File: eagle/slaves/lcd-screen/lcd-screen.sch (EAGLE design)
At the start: 25 parts, among them CON1 SPI, IC1 MCP1703CB, J1 RJ12RIGHTANGLE-I2C, J2 RJ12RIGHTANGLE-I2C, J3 RJ12RIGHTANGLE-I2C, U1 ATMEGA328P_TQFP

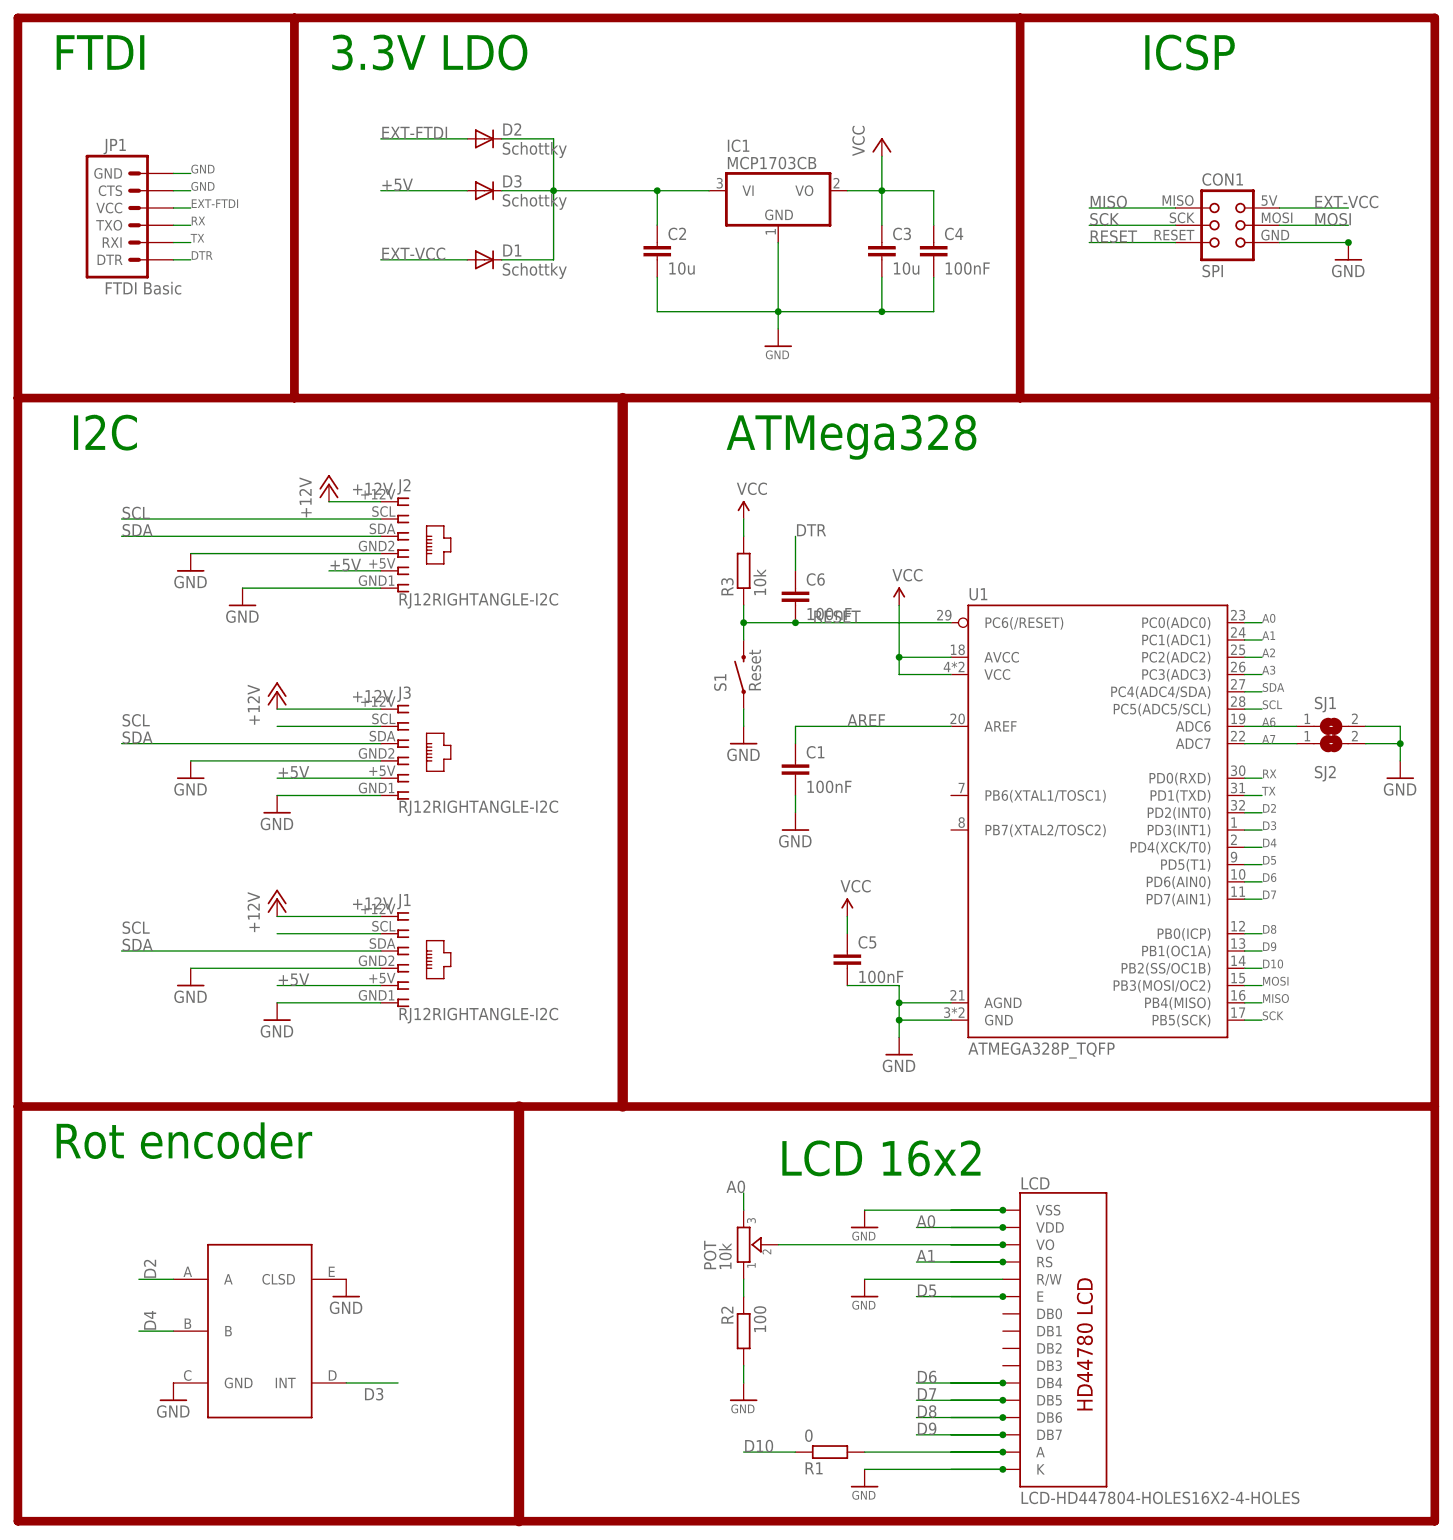
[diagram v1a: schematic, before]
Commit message: add crystal to bard
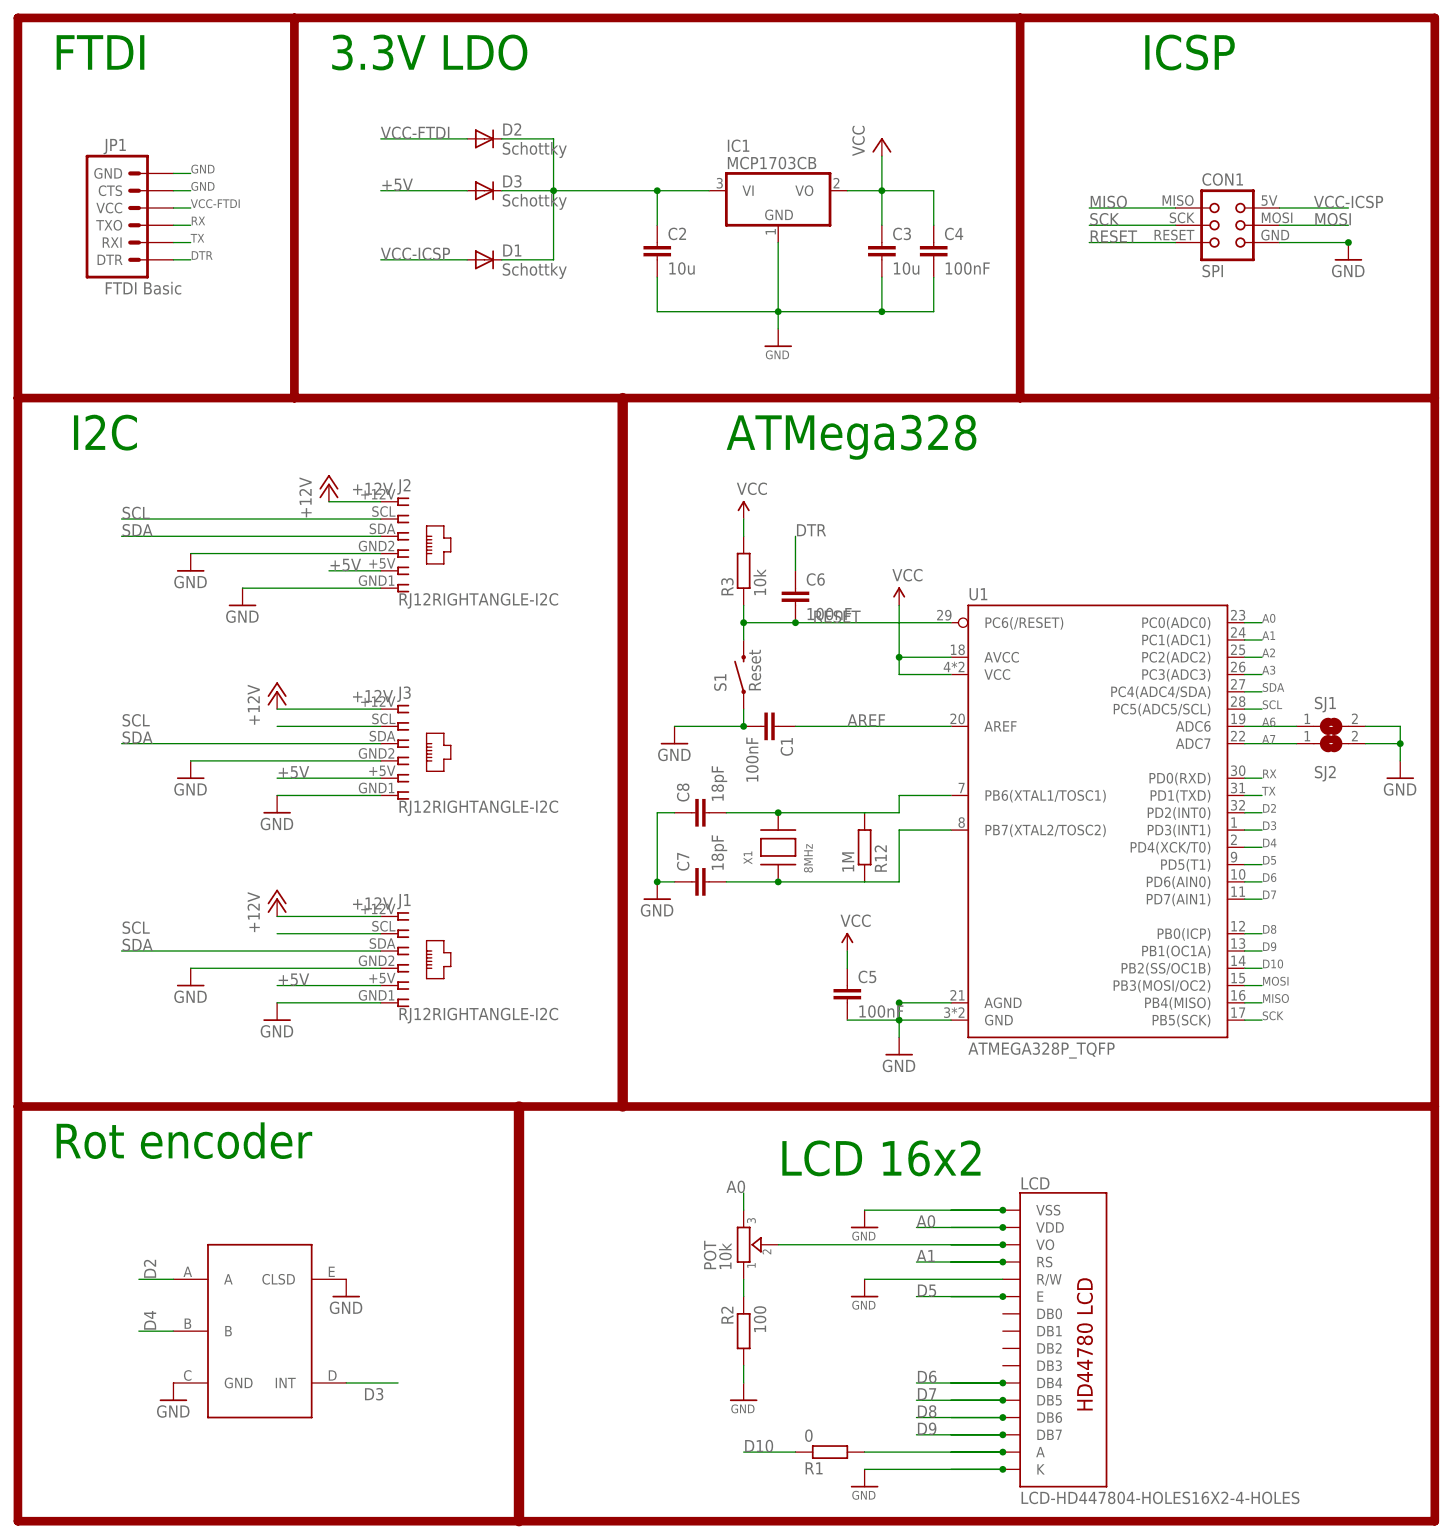
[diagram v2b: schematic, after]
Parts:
- added C7, C8: 18pF, rcl:C-EUC0805K
- added R12: 1M, rcl:R-EU_R0805
- added X1: 8MHz, lpatiny:XTALNX6035
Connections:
- net EXT-FTDI renamed VCC-FTDI
- net EXT-VCC renamed VCC-ICSP
- new net N$42: C8.2, R12.2, U1.PB6(XTAL1/TOSC1), X1.P$2
- new net XTAL1: C7.2, R12.1, U1.PB7(XTAL2/TOSC2), X1.P$1
- net GND: now also C7.1, C8.1
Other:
- moved on the sheet: C1, C5
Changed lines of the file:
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@@
 </part>
 <part name="GND3" library="SparkFun" deviceset="GND" device=""/>
-<part name="GND7" library="SparkFun" deviceset="GND" device=""/>
 <part name="P+11" library="SparkFun" deviceset="3.3V" device="" value="VCC"/>
 <part name="P+2" library="SparkFun" deviceset="3.3V" device="" value="VCC"/>
@@
 <part name="SJ2" library="jumper" library_urn="urn:adsk.eagle:library:252" deviceset="SJ" device="" package3d_urn="urn:adsk.eagle:package:15471/1"/>
 <part name="GND13" library="SparkFun" deviceset="GND" device=""/>
+<part name="C7" library="rcl" library_urn="urn:adsk.eagle:library:334" deviceset="C-EU" device="C0805K" package3d_urn="urn:adsk.eagle:package:23681/2" value="18pF">
+<attribute name="ELECROW" value="C1797"/>
+<attribute name="LCSC" value="C1797"/>
+<attribute name="MPN" value="77-VJ1206A180JXXPBC"/>
+</part>
+<part name="C8" library="rcl" library_urn="urn:adsk.eagle:library:334" deviceset="C-EU" device="C0805K" package3d_urn="urn:adsk.eagle:package:23681/2" value="18pF">
+<attribute name="ELECROW" value="C1797"/>
+<attribute name="LCSC" value="C1797"/>
+<attribute name="MPN" value="77-VJ1206A180JXXPBC"/>
+</part>
+<part name="X1" library="lpatiny" deviceset="XTAL" device="NX6035" value="8MHz">
+<attribute name="LCSC" value="C122522"/>
+<attribute name="MPN" value="729-F60800010"/>
+</part>
+<part name="GND39" library="supply1" deviceset="GND" device=""/>
+<part name="R12" library="rcl" deviceset="R-EU_" device="R0805" value="1M">
+<attribute name="ELECROW" value="C17514"/>
+<attribute name="LCSC" value="C17514"/>
+</part>
 </parts>
 <sheets>
@@
 <attribute name="LCSC" x="111.76" y="195.58" size="1.778" layer="96" display="off"/>
 </instance>
-<instance part="GND3" gate="1" x="106.68" y="114.3"/>
-<instance part="GND7" gate="1" x="114.3" y="101.6"/>
+<instance part="GND3" gate="1" x="96.52" y="114.3"/>
 <instance part="P+11" gate="G$1" x="106.68" y="147.32"/>
 <instance part="P+2" gate="G$1" x="129.54" y="134.62"/>
@@
 <attribute name="ELECROW" x="114.3" y="137.16" size="1.778" layer="96" display="off"/>
 </instance>
-<instance part="C1" gate="G$1" x="114.3" y="111.76">
-<attribute name="MPN" x="114.3" y="111.76" size="1.778" layer="96" display="off"/>
-<attribute name="LCSC" x="114.3" y="111.76" size="1.778" layer="96" display="off"/>
-<attribute name="ELECROW" x="114.3" y="111.76" size="1.778" layer="96" display="off"/>
-</instance>
-<instance part="C5" gate="G$1" x="121.92" y="83.82">
-<attribute name="MPN" x="121.92" y="83.82" size="1.778" layer="96" display="off"/>
-<attribute name="LCSC" x="121.92" y="83.82" size="1.778" layer="96" display="off"/>
-<attribute name="ELECROW" x="121.92" y="83.82" size="1.778" layer="96" display="off"/>
-</instance>
-<instance part="P+3" gate="G$1" x="121.92" y="88.9"/>
+<instance part="C1" gate="G$1" x="111.76" y="116.84" rot="R270">
+<attribute name="MPN" x="111.76" y="116.84" size="1.778" layer="96" rot="R270" display="off"/>
+<attribute name="LCSC" x="111.76" y="116.84" size="1.778" layer="96" rot="R270" display="off"/>
+<attribute name="ELECROW" x="111.76" y="116.84" size="1.778" layer="96" rot="R270" display="off"/>
+</instance>
+<instance part="C5" gate="G$1" x="121.92" y="78.74">
+<attribute name="MPN" x="121.92" y="78.74" size="1.778" layer="96" display="off"/>
+<attribute name="LCSC" x="121.92" y="78.74" size="1.778" layer="96" display="off"/>
+<attribute name="ELECROW" x="121.92" y="78.74" size="1.778" layer="96" display="off"/>
+</instance>
+<instance part="P+3" gate="G$1" x="121.92" y="83.82"/>
 <instance part="R3" gate="G$1" x="106.68" y="139.7" rot="R90">
 <attribute name="LCSC" x="106.68" y="139.7" size="1.778" layer="96" rot="R90" display="off"/>
@@
 </instance>
 <instance part="GND13" gate="1" x="203.2" y="109.22"/>
+<instance part="C7" gate="G$1" x="99.06" y="93.98" rot="R90">
+<attribute name="MPN" x="99.06" y="93.98" size="1.778" layer="96" rot="R90" display="off"/>
+<attribute name="LCSC" x="99.06" y="93.98" size="1.778" layer="96" rot="R90" display="off"/>
+<attribute name="ELECROW" x="99.06" y="93.98" size="1.778" layer="96" rot="R90" display="off"/>
+</instance>
+<instance part="C8" gate="G$1" x="99.06" y="104.14" rot="R90">
+<attribute name="MPN" x="99.06" y="104.14" size="1.778" layer="96" rot="R90" display="off"/>
+<attribute name="LCSC" x="99.06" y="104.14" size="1.778" layer="96" rot="R90" display="off"/>
+<attribute name="ELECROW" x="99.06" y="104.14" size="1.778" layer="96" rot="R90" display="off"/>
+</instance>
+<instance part="X1" gate="G$1" x="111.76" y="99.06" rot="R90">
+<attribute name="MPN" x="111.76" y="99.06" size="1.778" layer="96" rot="R90" display="off"/>
+<attribute name="LCSC" x="111.76" y="99.06" size="1.778" layer="96" rot="R90" display="off"/>
+</instance>
+<instance part="GND39" gate="1" x="93.98" y="91.44"/>
+<instance part="R12" gate="G$1" x="124.46" y="99.06" rot="MR90">
+<attribute name="ELECROW" x="124.46" y="99.06" size="1.778" layer="96" rot="MR90" display="off"/>
+<attribute name="LCSC" x="124.46" y="99.06" size="1.778" layer="96" rot="MR90" display="off"/>
+</instance>
 </instances>
 <busses>
@@
 </segment>
 <segment>
-<wire x1="106.68" y1="119.38" x2="106.68" y2="116.84" width="0.1524" layer="91"/>
 <pinref part="GND3" gate="1" pin="GND"/>
 <pinref part="S1" gate="G$1" pin="1"/>
-</segment>
-<segment>
-<wire x1="114.3" y1="104.14" x2="114.3" y2="106.68" width="0.1524" layer="91"/>
-<pinref part="GND7" gate="1" pin="GND"/>
 <pinref part="C1" gate="G$1" pin="2"/>
-</segment>
-<segment>
-<wire x1="129.54" y1="78.74" x2="129.54" y2="76.2" width="0.1524" layer="91"/>
+<wire x1="96.52" y1="116.84" x2="106.68" y2="116.84" width="0.1524" layer="91"/>
+<wire x1="106.68" y1="116.84" x2="106.68" y2="119.38" width="0.1524" layer="91"/>
+<junction x="106.68" y="116.84"/>
+</segment>
+<segment>
 <pinref part="GND5" gate="1" pin="GND"/>
 <pinref part="C5" gate="G$1" pin="2"/>
 <wire x1="129.54" y1="76.2" x2="129.54" y2="73.66" width="0.1524" layer="91"/>
 <wire x1="129.54" y1="73.66" x2="129.54" y2="71.12" width="0.1524" layer="91"/>
-<wire x1="129.54" y1="78.74" x2="121.92" y2="78.74" width="0.1524" layer="91"/>
+<wire x1="129.54" y1="73.66" x2="121.92" y2="73.66" width="0.1524" layer="91"/>
 <pinref part="U1" gate="U1" pin="GND"/>
 <wire x1="137.16" y1="73.66" x2="129.54" y2="73.66" width="0.1524" layer="91"/>
@@
 <wire x1="198.12" y1="114.3" x2="203.2" y2="114.3" width="0.1524" layer="91"/>
 <junction x="203.2" y="114.3"/>
+</segment>
+<segment>
+<pinref part="C8" gate="G$1" pin="1"/>
+<wire x1="96.52" y1="104.14" x2="93.98" y2="104.14" width="0.1524" layer="91"/>
+<pinref part="C7" gate="G$1" pin="1"/>
+<wire x1="93.98" y1="104.14" x2="93.98" y2="93.98" width="0.1524" layer="91"/>
+<wire x1="93.98" y1="93.98" x2="96.52" y2="93.98" width="0.1524" layer="91"/>
+<pinref part="GND39" gate="1" pin="GND"/>
+<junction x="93.98" y="93.98"/>
 </segment>
 </net>
@@
 <pinref part="C5" gate="G$1" pin="1"/>
 <pinref part="P+3" gate="G$1" pin="3.3V"/>
-<wire x1="121.92" y1="86.36" x2="121.92" y2="88.9" width="0.1524" layer="91"/>
+<wire x1="121.92" y1="81.28" x2="121.92" y2="83.82" width="0.1524" layer="91"/>
 </segment>
 </net>
@@
 <segment>
 <wire x1="137.16" y1="116.84" x2="114.3" y2="116.84" width="0.1524" layer="91"/>
-<wire x1="114.3" y1="116.84" x2="114.3" y2="114.3" width="0.1524" layer="91"/>
 <label x="121.92" y="116.84" size="1.778" layer="95"/>
 <pinref part="C1" gate="G$1" pin="1"/>
@@
 </segment>
 </net>
-<net name="EXT-VCC" class="0">
+<net name="VCC-ICSP" class="0">
 <segment>
 <pinref part="D1" gate="G$1" pin="A"/>
@@
 </segment>
 </net>
-<net name="EXT-FTDI" class="0">
+<net name="VCC-FTDI" class="0">
 <segment>
 <pinref part="D2" gate="G$1" pin="A"/>
@@
 </segment>
 </net>
+<net name="XTAL1" class="0">
+<segment>
+<pinref part="C7" gate="G$1" pin="2"/>
+<wire x1="124.46" y1="93.98" x2="111.76" y2="93.98" width="0.1524" layer="91"/>
+<wire x1="111.76" y1="93.98" x2="104.14" y2="93.98" width="0.1524" layer="91"/>
+<pinref part="X1" gate="G$1" pin="P$1"/>
+<junction x="111.76" y="93.98"/>
+<pinref part="R12" gate="G$1" pin="1"/>
+<pinref part="U1" gate="U1" pin="PB7(XTAL2/TOSC2)"/>
+<wire x1="137.16" y1="101.6" x2="129.54" y2="101.6" width="0.1524" layer="91"/>
+<wire x1="129.54" y1="101.6" x2="129.54" y2="93.98" width="0.1524" layer="91"/>
+<wire x1="129.54" y1="93.98" x2="124.46" y2="93.98" width="0.1524" layer="91"/>
+</segment>
+</net>
+<net name="N$42" class="0">
+<segment>
+<pinref part="C8" gate="G$1" pin="2"/>
+<wire x1="104.14" y1="104.14" x2="111.76" y2="104.14" width="0.1524" layer="91"/>
+<wire x1="111.76" y1="104.14" x2="124.46" y2="104.14" width="0.1524" layer="91"/>
+<pinref part="X1" gate="G$1" pin="P$2"/>
+<junction x="111.76" y="104.14"/>
+<pinref part="R12" gate="G$1" pin="2"/>
+<wire x1="124.46" y1="104.14" x2="129.54" y2="104.14" width="0.1524" layer="91"/>
+<wire x1="129.54" y1="104.14" x2="129.54" y2="106.68" width="0.1524" layer="91"/>
+<pinref part="U1" gate="U1" pin="PB6(XTAL1/TOSC1)"/>
+<wire x1="129.54" y1="106.68" x2="137.16" y2="106.68" width="0.1524" layer="91"/>
+</segment>
+</net>
